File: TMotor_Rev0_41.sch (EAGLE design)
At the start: 105 parts, among them U1 INA125U, U10 DEV-16771, U2 INA125U, U3 INA125U, U4 INA125U, U5 SN65HVD230MDREP, U6 2SJ305TE85LF, U7 2SJ305TE85LF, U8 2SJ305TE85LF, U9 2SJ305TE85LF

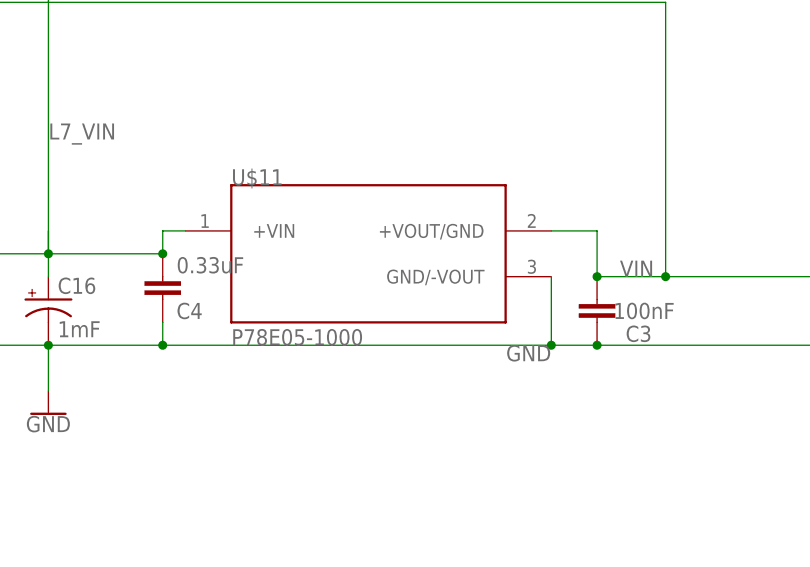
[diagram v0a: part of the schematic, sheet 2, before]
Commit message: fixed 5v regulator in rev 0.41
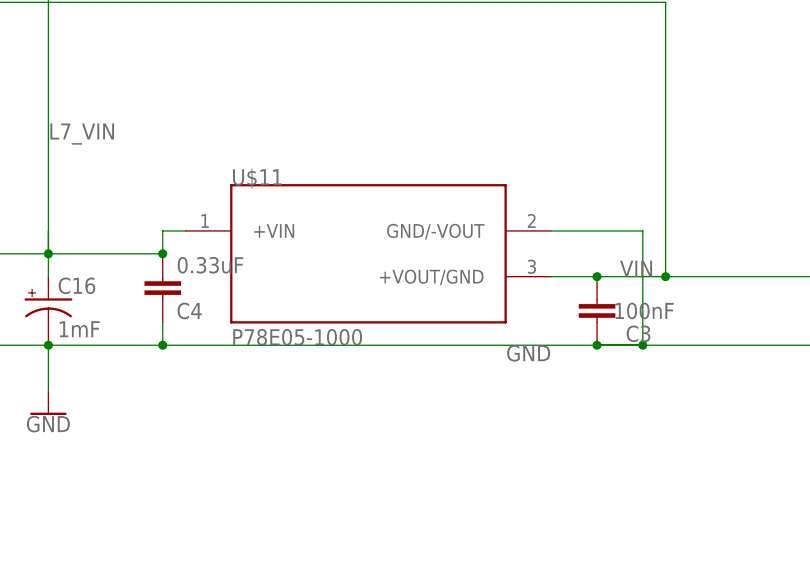
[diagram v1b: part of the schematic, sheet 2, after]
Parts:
- U$11: device SnapEDA-Library:P78E05-1000 -> SnapEDA-Library_Paul:P78E05-1000
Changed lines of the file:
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@@
 <part name="U$8" library="SnapEDA-Library" deviceset="FQP12P20" device=""/>
 <part name="U$10" library="SnapEDA-Library" deviceset="FQP12P20" device=""/>
-<part name="U$11" library="SnapEDA-Library" deviceset="P78E05-1000" device=""/>
+<part name="U$11" library="SnapEDA-Library_Paul" deviceset="P78E05-1000" device=""/>
 <part name="TEENSY_I2C" library="SparkFun-Connectors" library_urn="urn:adsk.eagle:library:513" deviceset="CONN_02" device="" package3d_urn="urn:adsk.eagle:package:38039/1"/>
 <part name="SPI2" library="con-lstb" library_urn="urn:adsk.eagle:library:162" deviceset="MA04-1" device="" package3d_urn="urn:adsk.eagle:package:8337/1"/>
@@
 <wire x1="-160.02" y1="157.48" x2="-160.02" y2="152.4" width="0.1524" layer="91"/>
 <wire x1="-71.12" y1="157.48" x2="-99.06" y2="157.48" width="0.1524" layer="91"/>
-<wire x1="-99.06" y1="157.48" x2="-104.14" y2="157.48" width="0.1524" layer="91"/>
+<wire x1="-99.06" y1="157.48" x2="-93.98" y2="157.48" width="0.1524" layer="91"/>
 <pinref part="C4" gate="G$1" pin="1"/>
-<wire x1="-104.14" y1="157.48" x2="-147.32" y2="157.48" width="0.1524" layer="91"/>
+<wire x1="-93.98" y1="157.48" x2="-147.32" y2="157.48" width="0.1524" layer="91"/>
 <wire x1="-147.32" y1="157.48" x2="-160.02" y2="157.48" width="0.1524" layer="91"/>
 <wire x1="-147.32" y1="160.02" x2="-147.32" y2="157.48" width="0.1524" layer="91"/>
@@
 <label x="-104.14" y="157.48" size="1.778" layer="95" rot="R180"/>
 <pinref part="U$11" gate="G$1" pin="GND/-VOUT"/>
-<wire x1="-104.14" y1="165.1" x2="-104.14" y2="157.48" width="0.1524" layer="91"/>
-<junction x="-104.14" y="157.48"/>
+<wire x1="-104.14" y1="170.18" x2="-93.98" y2="170.18" width="0.1524" layer="91"/>
+<wire x1="-93.98" y1="170.18" x2="-93.98" y2="157.48" width="0.1524" layer="91"/>
+<junction x="-93.98" y="157.48"/>
 </segment>
 <segment>
@@
 <pinref part="U$6" gate="G$1" pin="P$1"/>
 <pinref part="U$11" gate="G$1" pin="+VOUT/GND"/>
-<wire x1="-104.14" y1="170.18" x2="-99.06" y2="170.18" width="0.1524" layer="91"/>
-<wire x1="-99.06" y1="170.18" x2="-99.06" y2="165.1" width="0.1524" layer="91"/>
+<wire x1="-104.14" y1="165.1" x2="-99.06" y2="165.1" width="0.1524" layer="91"/>
 <junction x="-99.06" y="165.1"/>
 </segment>
